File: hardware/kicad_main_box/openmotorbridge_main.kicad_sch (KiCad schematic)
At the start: 0 parts

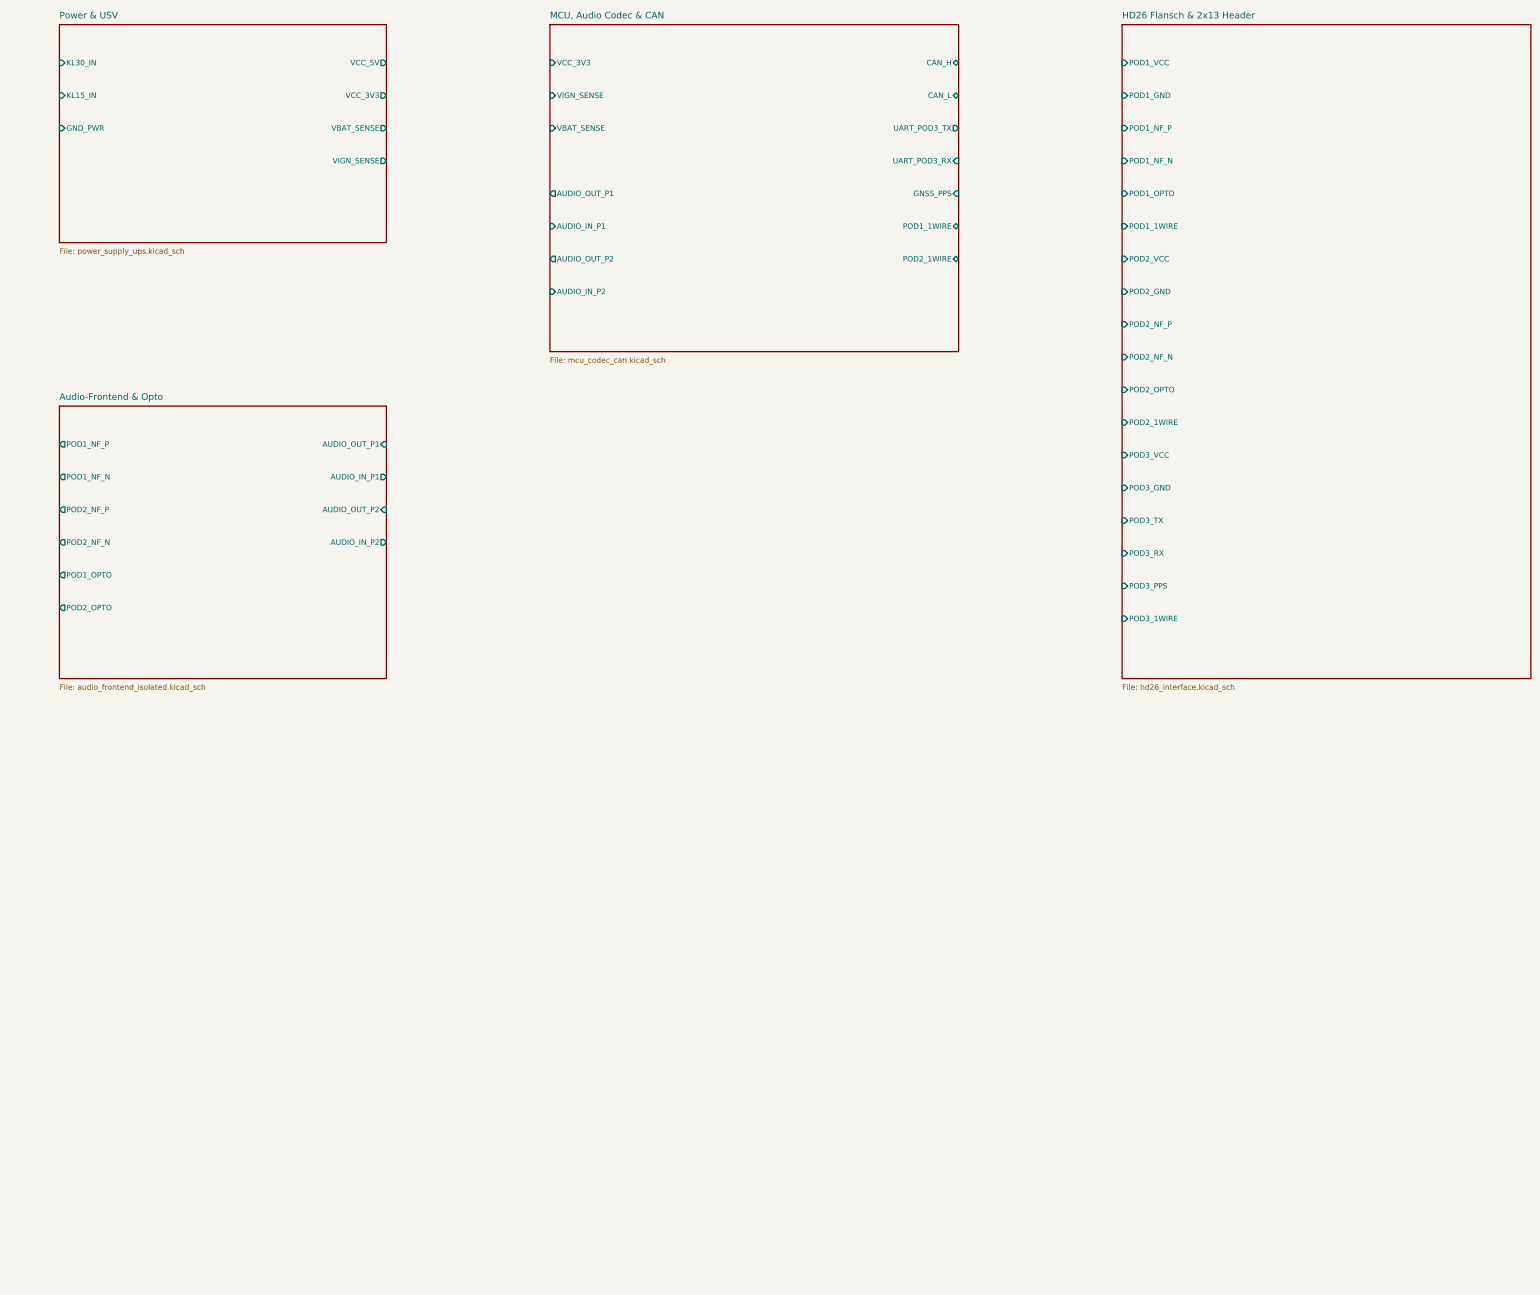
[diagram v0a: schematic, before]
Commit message: feat(hw): finalize PCB lineup routing, sync PCBA 03 cartridge with J_PROG header and DTM12 schematics
- PCBA 01 (Central Box): Remediate net routing, DTM12 hierarchical schematic synchronization, 100% routed, 0 DRC errors.
- PCBA 03 (Smart Modular Cartridge): Position and route J_PROG 4-pin SMD programming header on F.Cu at (108.0, 89.61), synchronize CPL and schematic, 100% routed, 0 DRC errors.
- PCBA 05 (Universal Front Node): Preconnect and routing verified, 100% routed, 0 DRC errors.
- PCBA 07 (LoRa Smart-Keyfob): Routing and DRC verified, 100% routed, 0 DRC errors.
- PCBA 08 (Radar 2.0 Sub-MCU & Wings): Sub-MCU routing and HF isolation verified, 100% routed, 0 DRC errors.
- PCBA 10 (OMM 446 PMR/DMR Intercom): KiCad DRC verified, 100% routed, 0 DRC errors.
- Firmware: Align configuration headers across front_node and smart_cartridge.
- Tools: Add comprehensive preflight PCBA audit suite tools/audit_pcbas_preflight.py.
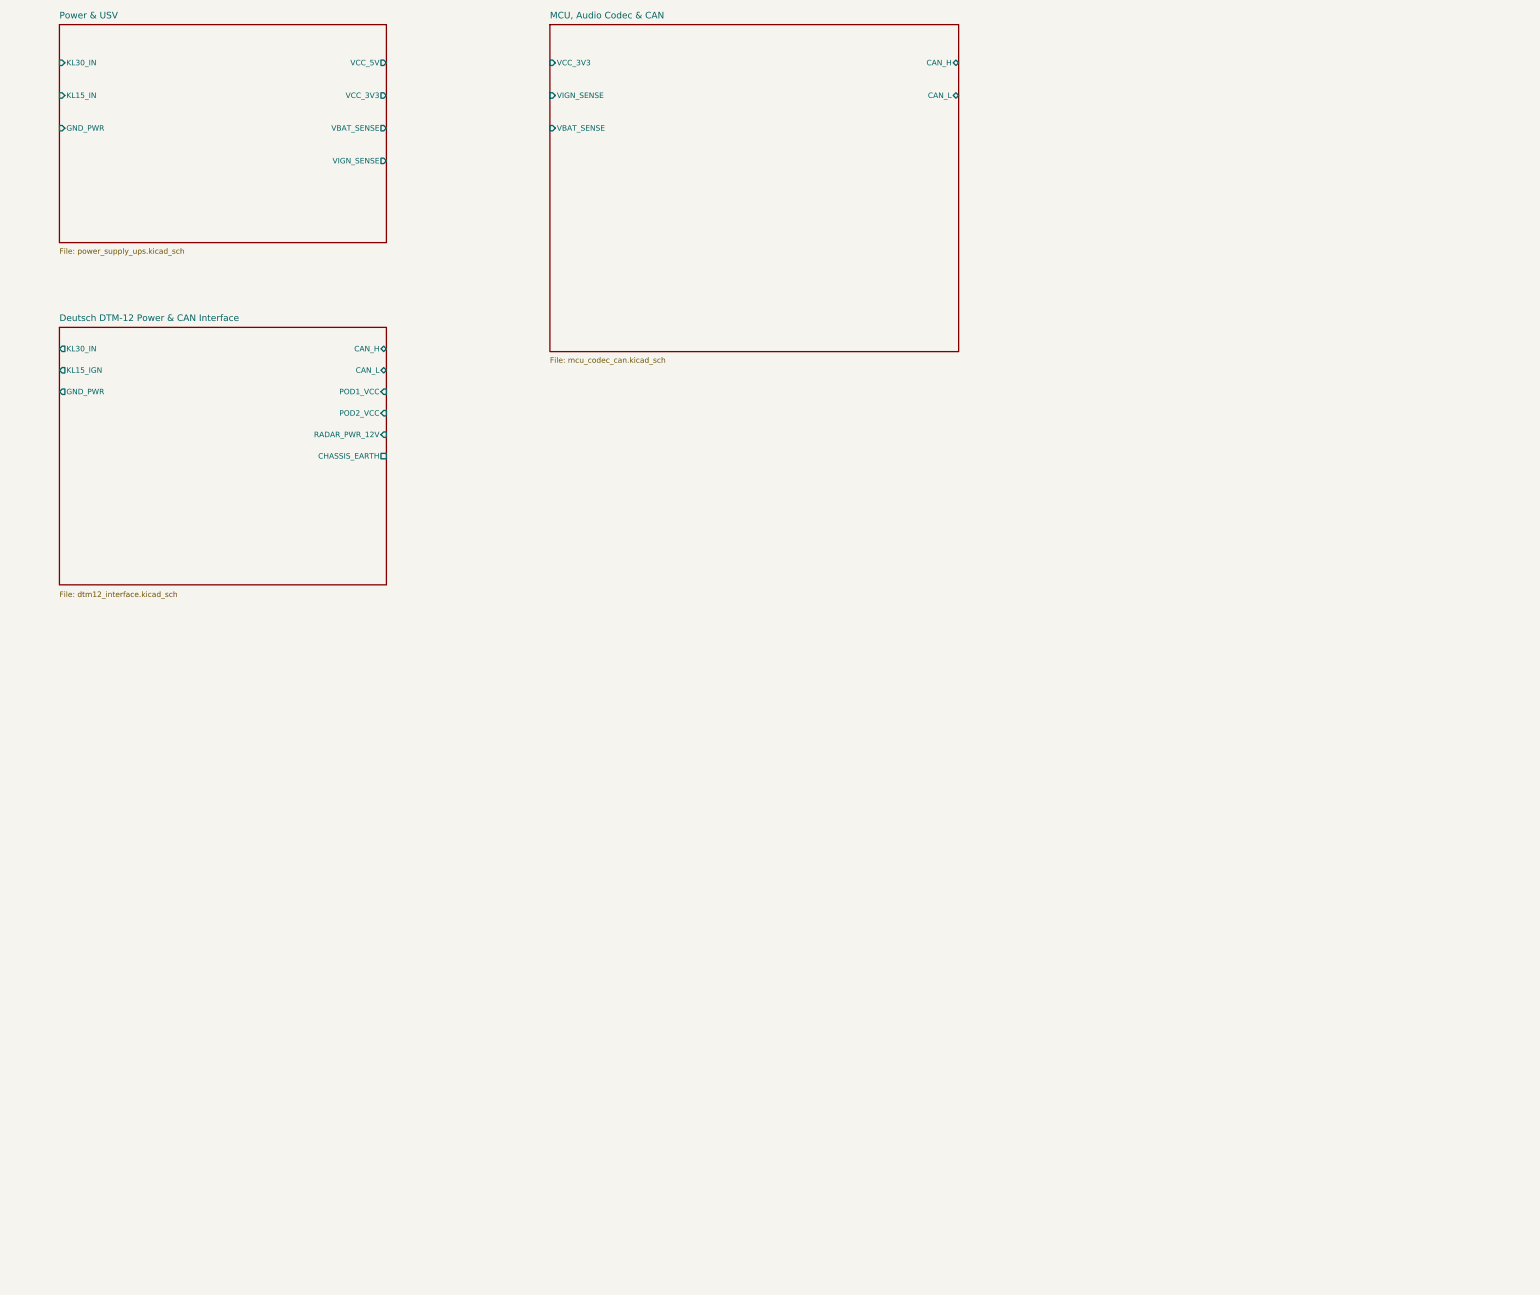
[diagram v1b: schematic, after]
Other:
- sheet HD26 Flansch & 2x13 Header renamed Deutsch DTM-12 Power & CAN Interface
- removed sheet Audio-Frontend & Opto
- sheet Deutsch DTM-12 Power & CAN Interface: file hd26_interface.kicad_sch -> dtm12_interface.kicad_sch
- sheet Deutsch DTM-12 Power & CAN Interface ports: added CAN_H, CAN_L, CHASSIS_EARTH, GND_PWR, KL15_IGN, KL30_IN, RADAR_PWR_12V; removed POD1_1WIRE, POD1_GND, POD1_NF_N, POD1_NF_P, POD1_OPTO, POD2_1WIRE, POD2_GND, POD2_NF_N, POD2_NF_P, POD2_OPTO, POD3_1WIRE, POD3_GND, POD3_PPS, POD3_RX, POD3_TX, POD3_VCC
- sheet MCU, Audio Codec & CAN ports: added none; removed AUDIO_IN_P1, AUDIO_IN_P2, AUDIO_OUT_P1, AUDIO_OUT_P2, GNSS_PPS, POD1_1WIRE, POD2_1WIRE, UART_POD3_RX, UART_POD3_TX
- title: OpenMotorBridge v8.0 - Zentralbox Top-Level Blockschaltbild -> OpenMotorBridge v9.6 - Zentralbox Top-Level Blockschaltbild

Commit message: fix(hardware): fleet-wide 7-PCBA remediation, schematic parity & doc alignment
- PCBA 01 (Central Box): Synchronized DTM-12 schematic and PCB routing, purged obsolete analog audio transformers/HD26 connector.
- PCBA 03 (Smart Cartridge): Verified Kelvin ground isolation on J_AUDIO_PWR, resolved U1.16 BAY_SELECT single net.
- PCBA 05 (Front Node): Mapped DW3110 UWB SPI/IRQ/RST to ESP32-S3 pads 30-35, connected MK1 I2S MEMS mic and Y_UWB crystal.
- PCBA 07 (Smart Keyfob): Connected 12 unrouted signals (SX1262 LoRa SPI, DRV2605L I2C, SWD, RTC crystal, buttons) to nRF52840 pads.
- PCBA 08 (Radar Sub-MCU): Synchronized J1.1 power rail to VCC_5V, connected Y1_UWB crystal to DW3110 pads 4 & 5.
- PCBA 09 & PCBA 10 (OMM 2.4 GHz & 446 MHz): Verified 4-layer stackup, BQ24075 ground ties, SA818 isolation, and vertical B.Cu J_HELMET orientation.
- Tools: Added verify_hardware_integrity.py with automated DRC/parity/single-net/floating-pad checks (all 7 PCBAs HEALTHY).
- Docs: Synchronized docs/de and docs/en hardware specifications, pinouts, and DTM-12 architecture.
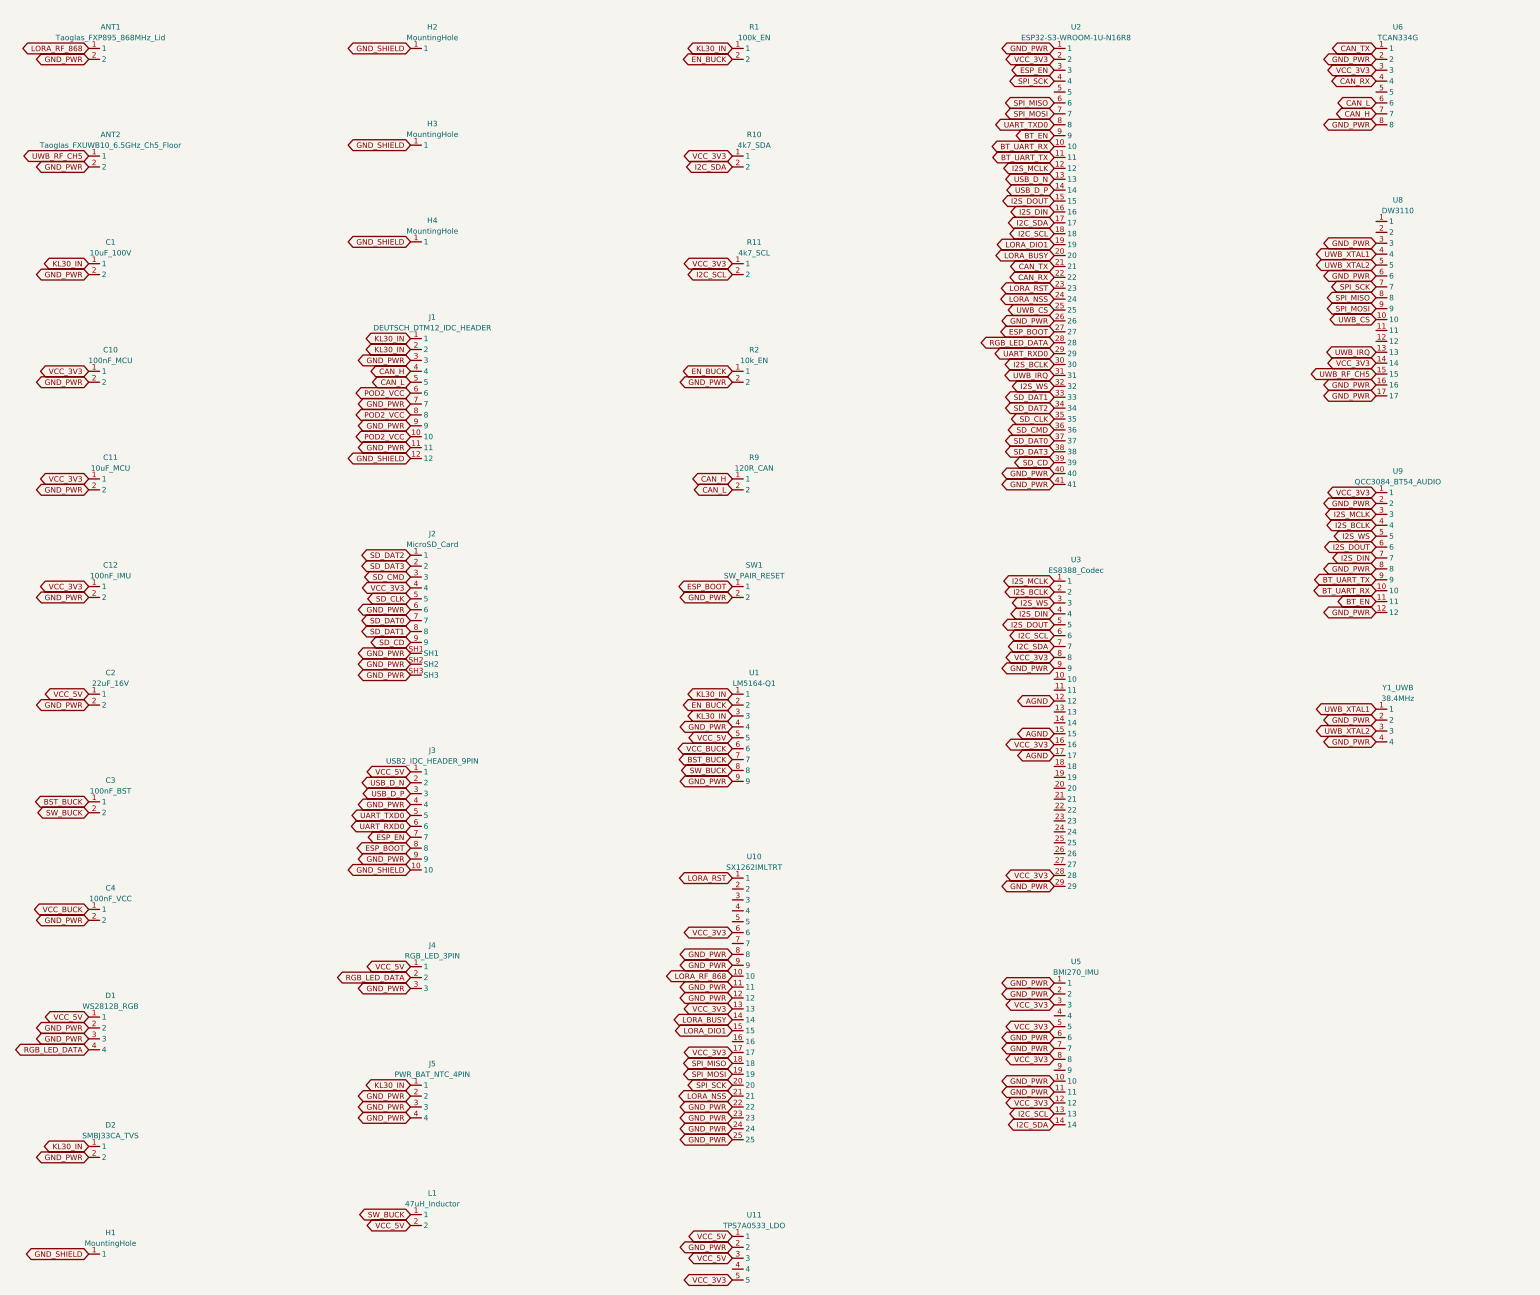
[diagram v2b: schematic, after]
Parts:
- added ANT1: Taoglas_FXP895_868MHz_Lid, U.FL_Hirose_U.FL-R-SMT-1_Vertical, symbol OMB_Main:ANT1_Taoglas_FXP895_868MHz_Lid
- added ANT2: Taoglas_FXUWB10_6.5GHz_Ch5_Floor, U.FL_Hirose_U.FL-R-SMT-1_Vertical, symbol OMB_Main:ANT2_Taoglas_FXUWB10_6.5GHz_Ch5_Floor
- added C1: 10uF_100V, Capacitor_SMD:C_0805_2012Metric, symbol OMB_Main:C1_10uF_100V
- added C10: 100nF_MCU, Capacitor_SMD:C_0603_1608Metric, symbol OMB_Main:C10_100nF_MCU
- added C11: 10uF_MCU, Capacitor_SMD:C_0805_2012Metric, symbol OMB_Main:C11_10uF_MCU
- added C12: 100nF_IMU, Capacitor_SMD:C_0603_1608Metric, symbol OMB_Main:C12_100nF_IMU
- added C2: 22uF_16V, Capacitor_SMD:C_0805_2012Metric, symbol OMB_Main:C2_22uF_16V
- added C3: 100nF_BST, Capacitor_SMD:C_0603_1608Metric, symbol OMB_Main:C3_100nF_BST
- added C4: 100nF_VCC, Capacitor_SMD:C_0603_1608Metric, symbol OMB_Main:C4_100nF_VCC
- added D1: WS2812B_RGB, LED_SMD:LED_WS2812B-2020, symbol OMB_Main:D1_WS2812B_RGB
- added D2: SMBJ33CA_TVS, Diode_SMD:D_SMB, symbol OMB_Main:D2_SMBJ33CA_TVS
- added H1: MountingHole, MountingHole:MountingHole_3.2mm_M3_Pad_Via, symbol OMB_Main:H1_MountingHole
- added H2: MountingHole, MountingHole:MountingHole_3.2mm_M3_Pad_Via, symbol OMB_Main:H2_MountingHole
- added H3: MountingHole, MountingHole:MountingHole_3.2mm_M3_Pad_Via, symbol OMB_Main:H3_MountingHole
- added H4: MountingHole, MountingHole:MountingHole_3.2mm_M3_Pad_Via, symbol OMB_Main:H4_MountingHole
- added J1: DEUTSCH_DTM12_IDC_HEADER, Connector_IDC:IDC-Header_2x06_P2.54mm_Vertical, symbol OMB_Main:J1_DEUTSCH_DTM12_IDC_HEADER
- added J2: MicroSD_Card, Connector_Card:microSD_HC_Hirose_DM3D-SF, symbol OMB_Main:J2_MicroSD_Card
- added J3: USB2_IDC_HEADER_9PIN, Connector_IDC:IDC-Header_2x05_P2.54mm_Vertical, symbol OMB_Main:J3_USB2_IDC_HEADER_9PIN
- added J4: RGB_LED_3PIN, Connector_JST:JST_PH_B3B-PH-K_1x03_P2.00mm_Vertical, symbol OMB_Main:J4_RGB_LED_3PIN
- added J5: PWR_BAT_NTC_4PIN, Connector_JST:JST_PH_B4B-PH-K_1x04_P2.00mm_Vertical, symbol OMB_Main:J5_PWR_BAT_NTC_4PIN
- added L1: 47uH_Inductor, Inductor_SMD:L_Sunlord_MWSA1206S-470, symbol OMB_Main:L1_47uH_Inductor
- added R1: 100k_EN, Resistor_SMD:R_0603_1608Metric, symbol OMB_Main:R1_100k_EN
- added R10: 4k7_SDA, Resistor_SMD:R_0603_1608Metric, symbol OMB_Main:R10_4k7_SDA
- added R11: 4k7_SCL, Resistor_SMD:R_0603_1608Metric, symbol OMB_Main:R11_4k7_SCL
- added R2: 10k_EN, Resistor_SMD:R_0603_1608Metric, symbol OMB_Main:R2_10k_EN
- added R9: 120R_CAN, Resistor_SMD:R_0603_1608Metric, symbol OMB_Main:R9_120R_CAN
- added SW1: SW_PAIR_RESET, SW_Push_SPST_NO_Alps_SKRK, symbol OMB_Main:SW1_SW_PAIR_RESET
- added U1: LM5164-Q1, Package_SO:SOIC-8-1EP_3.9x4.9mm_P1.27mm_EP2.41x3.3mm, symbol OMB_Main:U1_LM5164-Q1
- added U10: SX1262IMLTRT, QFN-24-1EP_4x4mm_P0.5mm_EP2.8x2.8mm, symbol OMB_Main:U10_SX1262IMLTRT
- added U11: TPS7A0533_LDO, Package_TO_SOT_SMD:SOT-23-5, symbol OMB_Main:U11_TPS7A0533_LDO
- added U2: ESP32-S3-WROOM-1U-N16R8, ESP32-S3-WROOM-1U, symbol OMB_Main:U2_ESP32-S3-WROOM-1U-N16R8
- added U3: ES8388_Codec, Package_DFN_QFN:QFN-28-1EP_4x4mm_P0.4mm_EP2.4x2.4mm, symbol OMB_Main:U3_ES8388_Codec
- added U5: BMI270_IMU, Package_LGA:LGA-14_2.5x3mm_P0.5mm, symbol OMB_Main:U5_BMI270_IMU
- added U6: TCAN334G, Package_SO:SOIC-8_3.9x4.9mm_P1.27mm, symbol OMB_Main:U6_TCAN334G
- added U8: DW3110, QFN-16-1EP_3x3mm_P0.5mm_EP1.7x1.7mm_ThermalVias, symbol OMB_Main:U8_DW3110
- added U9: QCC3084_BT54_AUDIO, RF_Module:Qualcomm_QCC3084_Module, symbol OMB_Main:U9_QCC3084_BT54_AUDIO
- added Y1_UWB: 38.4MHz, Crystal:Crystal_SMD_2016-4Pin_2.0x1.6mm, symbol OMB_Main:Y1_UWB_38.4MHz
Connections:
- new net AGND: U3.12, U3.15, U3.17
- new net BST_BUCK: C3.1, U1.7
- new net BT_EN: U2.9, U9.11
- new net BT_UART_RX: U2.10, U9.10
- new net BT_UART_TX: U2.11, U9.9
- new net CAN_H: J1.4, R9.1, U6.7
- new net CAN_L: J1.5, R9.2, U6.6
- new net CAN_RX: U2.22, U6.4
- new net CAN_TX: U2.21, U6.1
- new net EN_BUCK: R1.2, R2.1, U1.2
- new net ESP_BOOT: J3.8, SW1.1, U2.27
- new net ESP_EN: J3.7, U2.3
- new net GND_PWR: ANT1.2, ANT2.2, C1.2, C10.2, C11.2, C12.2, C2.2, C4.2, D1.2, D1.3, D2.2, J1.11, J1.3, J1.7, J1.9, J2.6, J2.SH1, J2.SH2, J2.SH3, J3.4, J3.9, J4.3, J5.2, J5.3, J5.4, R2.2, SW1.2, U1.4, U1.9, U10.11, U10.12, U10.22, U10.23, U10.24, U10.25, U10.8, U10.9, U11.2, U2.1, U2.26, U2.40, U2.41, U3.29, U3.9, U5.1, U5.10, U5.11, U5.2, U5.6, U5.7, U6.2, U6.8, U8.16, U8.17, U8.3, U8.6, U9.12, U9.2, U9.8, Y1_UWB.2, Y1_UWB.4
- new net GND_SHIELD: H1.1, H2.1, H3.1, H4.1, J1.12, J3.10
- new net I2C_SCL: R11.2, U2.18, U3.6, U5.13
- new net I2C_SDA: R10.2, U2.17, U3.7, U5.14
- new net I2S_BCLK: U2.30, U3.2, U9.4
- new net I2S_DIN: U2.16, U3.4, U9.7
- new net I2S_DOUT: U2.15, U3.5, U9.6
- new net I2S_MCLK: U2.12, U3.1, U9.3
- new net I2S_WS: U2.32, U3.3, U9.5
- new net KL30_IN: C1.1, D2.1, J1.1, J1.2, J5.1, R1.1, U1.1, U1.3
- new net LORA_BUSY: U10.14, U2.20
- new net LORA_DIO1: U10.15, U2.19
- new net LORA_NSS: U10.21, U2.24
- new net LORA_RF_868: ANT1.1, U10.10
- new net LORA_RST: U10.1, U2.23
- new net POD2_VCC: J1.10, J1.6, J1.8
- new net RGB_LED_DATA: D1.4, J4.2, U2.28
- new net SD_CD: J2.9, U2.39
- new net SD_CLK: J2.5, U2.35
- new net SD_CMD: J2.3, U2.36
- new net SD_DAT0: J2.7, U2.37
- new net SD_DAT1: J2.8, U2.33
- new net SD_DAT2: J2.1, U2.34
- new net SD_DAT3: J2.2, U2.38
- new net SPI_MISO: U10.18, U2.6, U8.8
- new net SPI_MOSI: U10.19, U2.7, U8.9
- new net SPI_SCK: U10.20, U2.4, U8.7
- new net SW_BUCK: C3.2, L1.1, U1.8
- new net UART_RXD0: J3.6, U2.29
- new net UART_TXD0: J3.5, U2.8
- new net USB_D_N: J3.2, U2.13
- new net USB_D_P: J3.3, U2.14
- new net UWB_CS: U2.25, U8.10
- new net UWB_IRQ: U2.31, U8.13
- new net UWB_RF_CH5: ANT2.1, U8.15
- new net UWB_XTAL1: U8.4, Y1_UWB.1
- new net UWB_XTAL2: U8.5, Y1_UWB.3
- new net VCC_3V3: C10.1, C11.1, C12.1, J2.4, R10.1, R11.1, U10.13, U10.17, U10.6, U11.5, U2.2, U3.16, U3.28, U3.8, U5.12, U5.3, U5.5, U5.8, U6.3, U8.14, U9.1
- new net VCC_5V: C2.1, D1.1, J3.1, J4.1, L1.2, U1.5, U11.1, U11.3
- new net VCC_BUCK: C4.1, U1.6
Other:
- removed sheet Deutsch DTM-12 Power & CAN Interface
- removed sheet MCU, Audio Codec & CAN
- removed sheet Power & USV
- title: OpenMotorBridge v9.6 - Zentralbox Top-Level Blockschaltbild -> OpenMotorBridge v9.6 - Zentralbox Central Unit (PCBA 01)
